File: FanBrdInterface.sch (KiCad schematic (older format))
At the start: 14 parts, among them J13 FanBrdConn, U14 SI8261ABC-IS, U15 SI8261ABC-IS, U16 SI8261ABC-IS, U17 SI8261ABC-IS

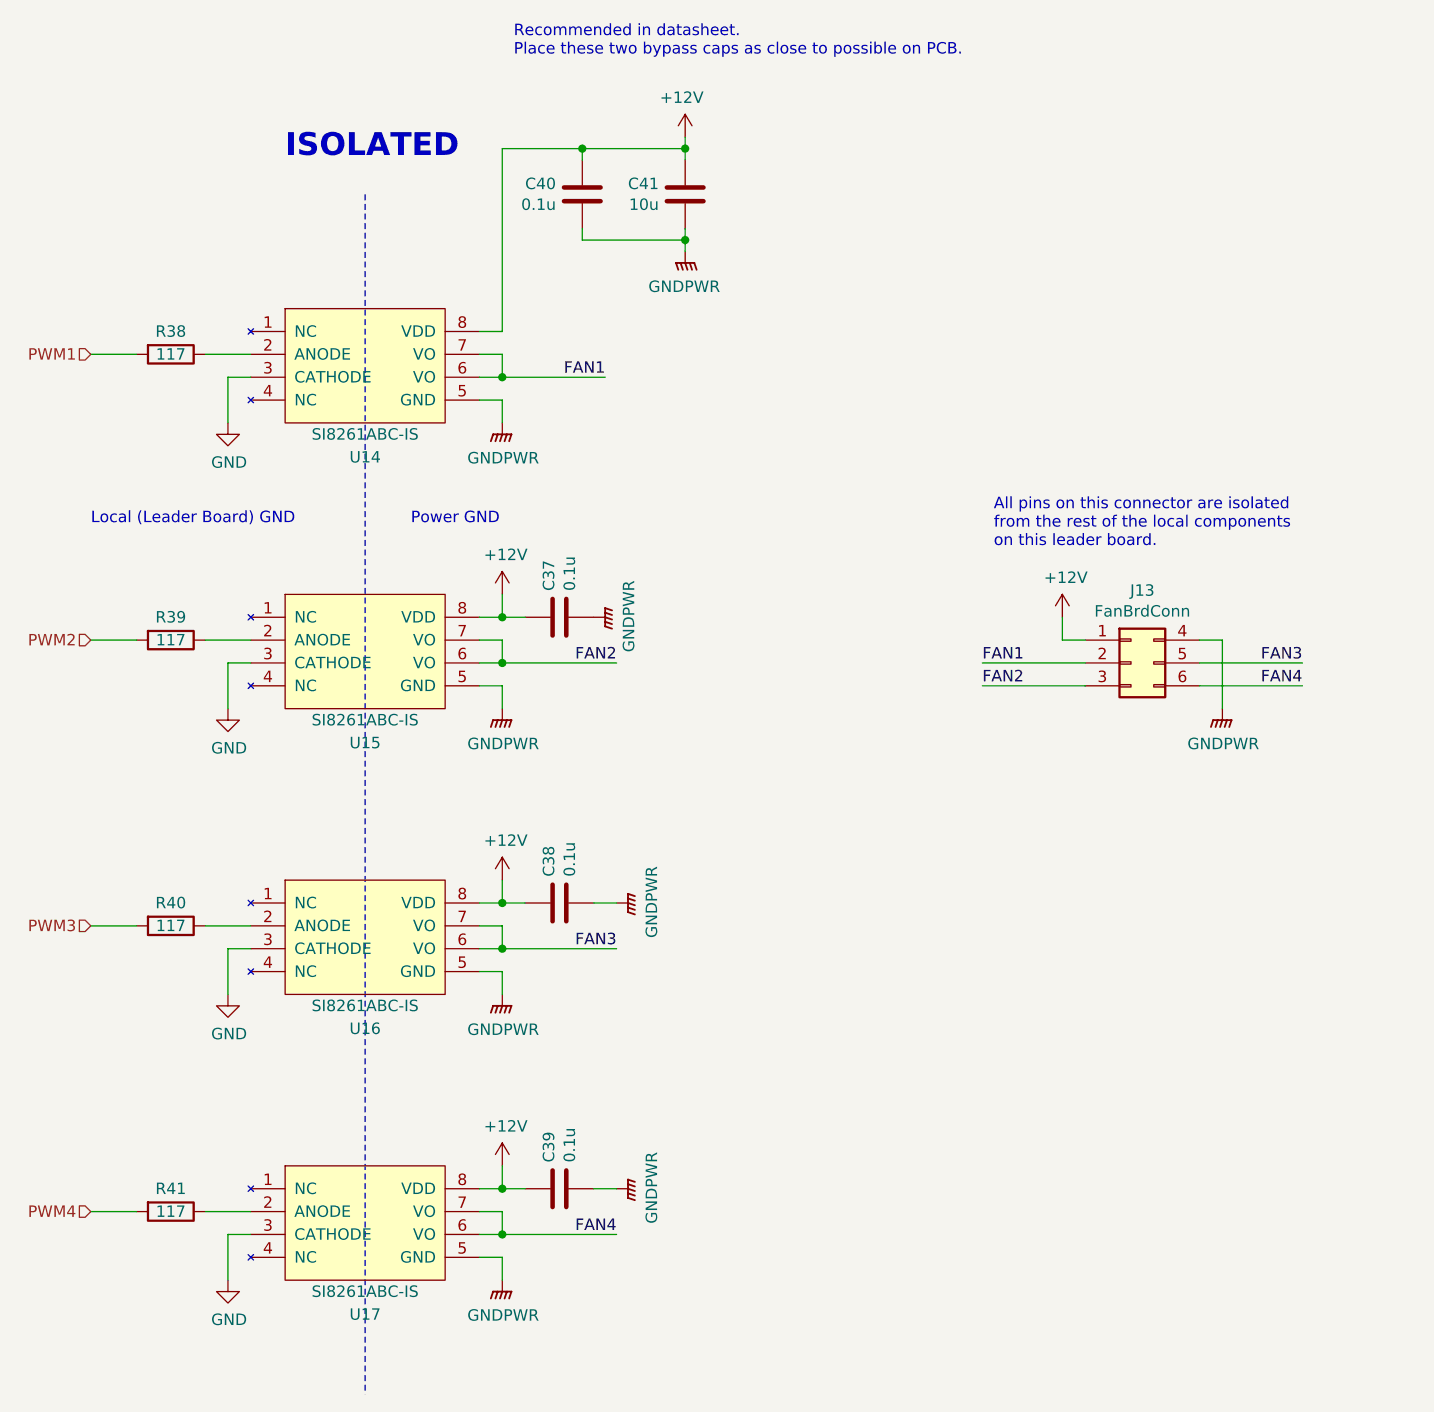
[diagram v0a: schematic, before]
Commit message: Moves BAS70-04 to utsvt-chips because other systems use this component
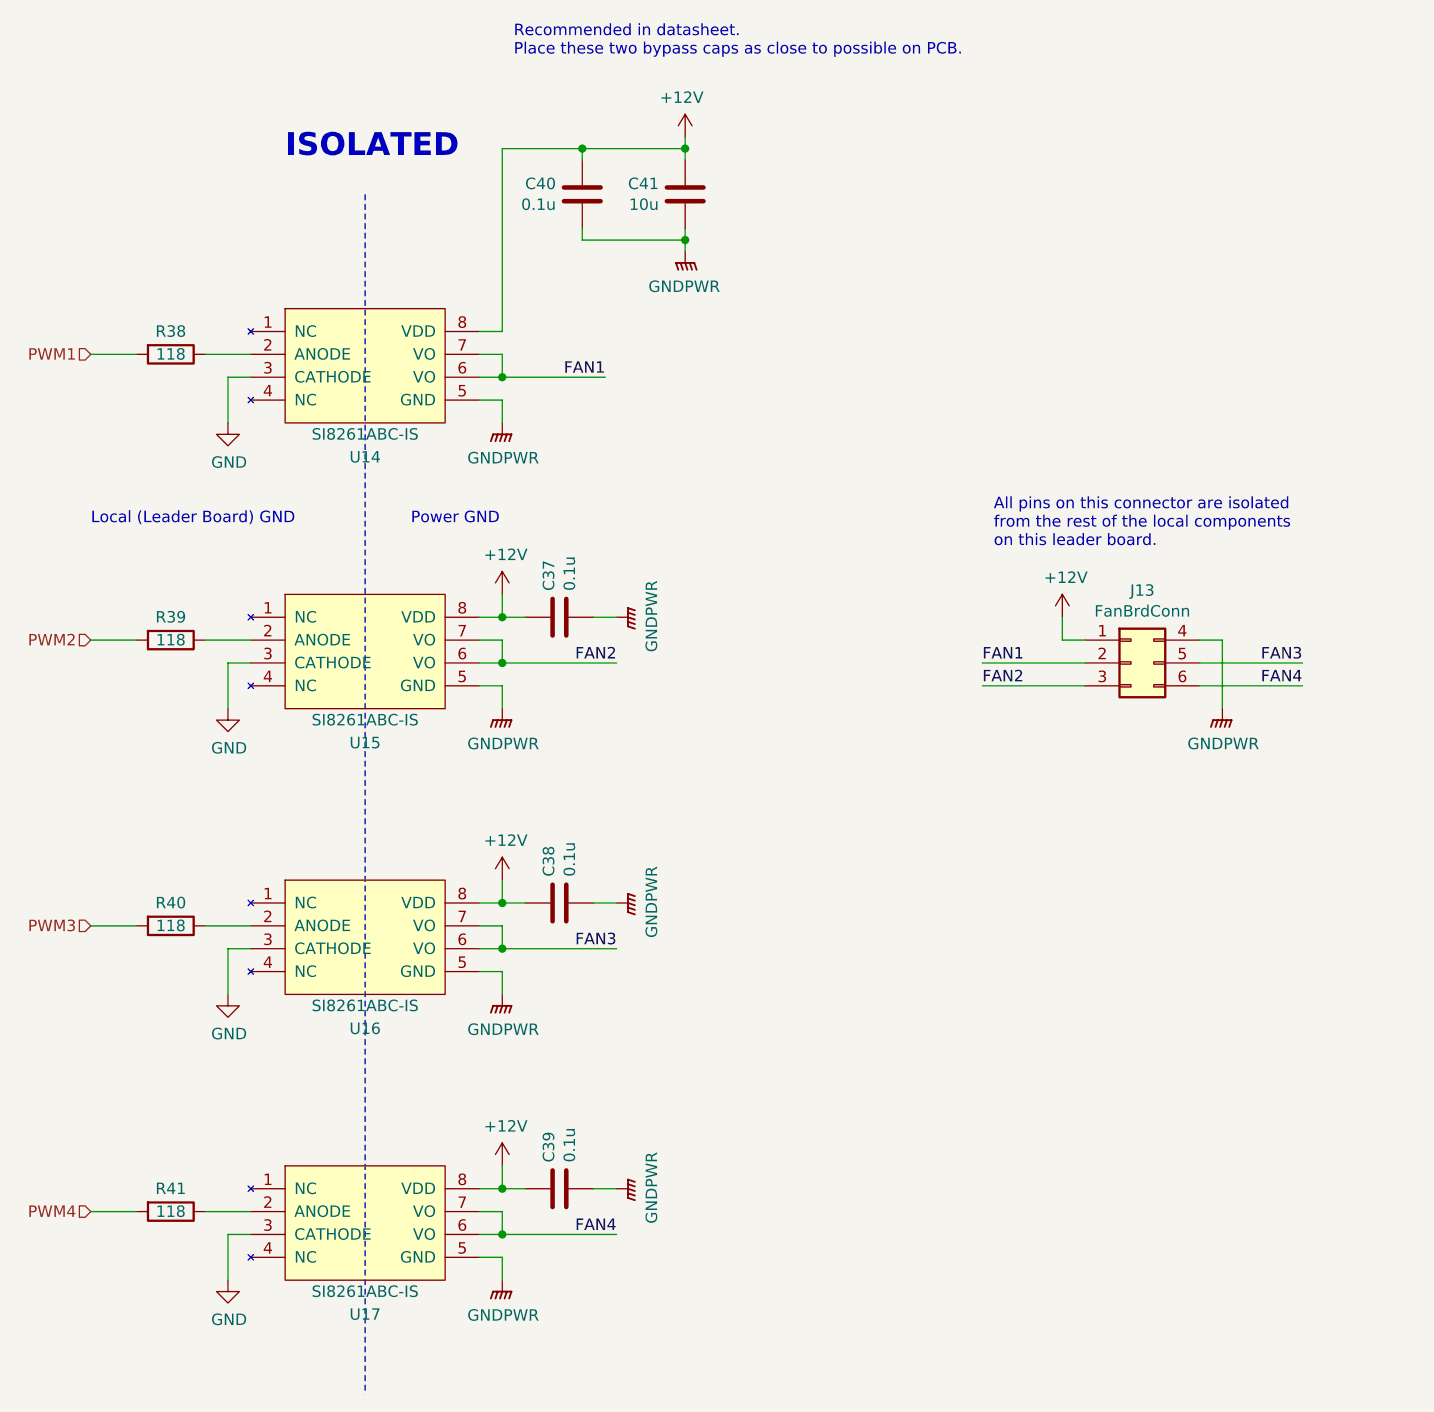
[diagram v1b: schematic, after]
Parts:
- R38, R39, R40, R41: value 117 -> 118
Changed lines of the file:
@@
 P 3400 2700
 F 0 "R38" V 3300 2700 50  0000 C CNN
-F 1 "117" V 3400 2700 50  0000 C CNN
+F 1 "118" V 3400 2700 50  0000 C CNN
 F 2 "Resistor_SMD:R_0805_2012Metric" V 3330 2700 50  0001 C CNN
 F 3 "~" H 3400 2700 50  0001 C CNN
@@
 P 3400 3950
 F 0 "R39" V 3300 3950 50  0000 C CNN
-F 1 "117" V 3400 3950 50  0000 C CNN
+F 1 "118" V 3400 3950 50  0000 C CNN
 F 2 "Resistor_SMD:R_0805_2012Metric" V 3330 3950 50  0001 C CNN
 F 3 "~" H 3400 3950 50  0001 C CNN
@@
 P 3400 5200
 F 0 "R40" V 3300 5200 50  0000 C CNN
-F 1 "117" V 3400 5200 50  0000 C CNN
+F 1 "118" V 3400 5200 50  0000 C CNN
 F 2 "Resistor_SMD:R_0805_2012Metric" V 3330 5200 50  0001 C CNN
 F 3 "~" H 3400 5200 50  0001 C CNN
@@
 P 3400 6450
 F 0 "R41" V 3300 6450 50  0000 C CNN
-F 1 "117" V 3400 6450 50  0000 C CNN
+F 1 "118" V 3400 6450 50  0000 C CNN
 F 2 "Resistor_SMD:R_0805_2012Metric" V 3330 6450 50  0001 C CNN
 F 3 "~" H 3400 6450 50  0001 C CNN
@@
 L power:GNDPWR #PWR?
 U 1 1 5F1DA30D
-P 5250 3850
+P 5350 3850
 AR Path="/5C38C674/5F1DA30D" Ref="#PWR?"  Part="1"
 AR Path="/5F145F02/5F1DA30D" Ref="#PWR091"  Part="1"
-F 0 "#PWR091" H 5250 3650 50  0001 C CNN
-F 1 "GNDPWR" H 5254 3696 50  0000 C CNN
-F 2 "" H 5250 3800 50  0001 C CNN
-F 3 "" H 5250 3800 50  0001 C CNN
-	1    5250 3850
+F 0 "#PWR091" H 5350 3650 50  0001 C CNN
+F 1 "GNDPWR" H 5354 3696 50  0000 C CNN
+F 2 "" H 5350 3800 50  0001 C CNN
+F 3 "" H 5350 3800 50  0001 C CNN
+	1    5350 3850
 	0    -1   -1   0
 $EndComp
@@
 Text Notes 4450 3450 0    50   ~ 0
 Power GND
+Wire Wire Line
+	5350 3850 5250 3850
 $EndSCHEMATC

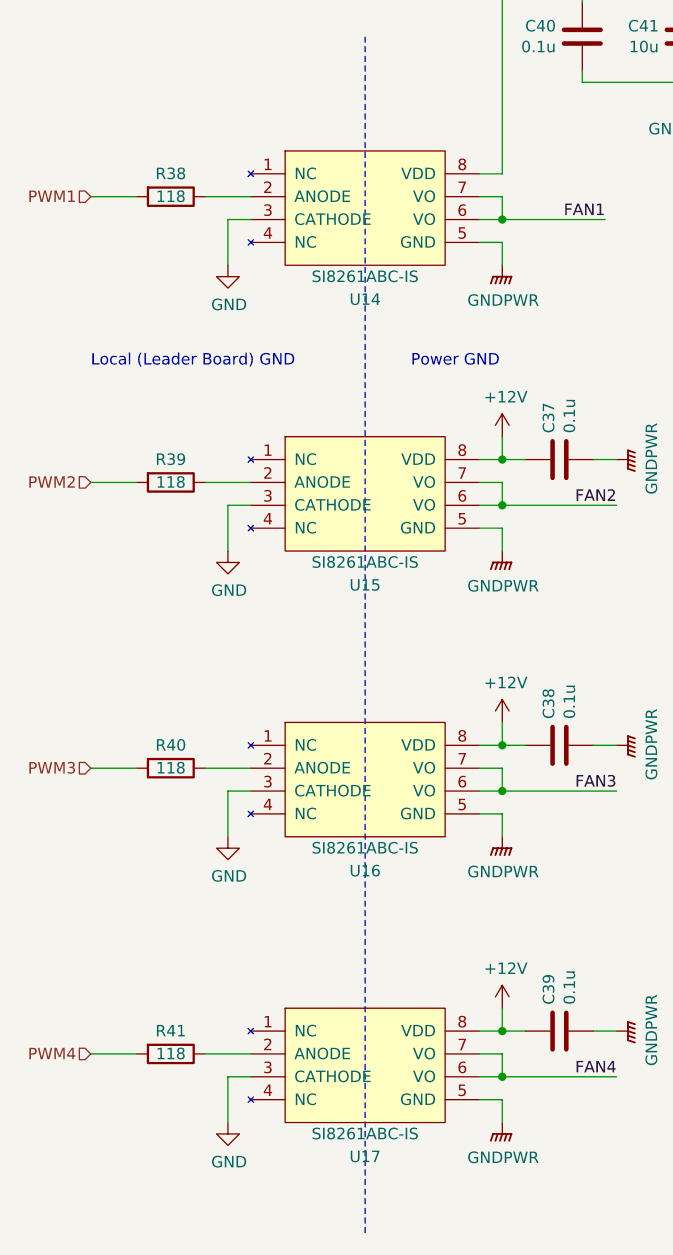
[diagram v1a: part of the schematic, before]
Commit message: Updates BAS70-04 footprint for Contactor auxillary interface
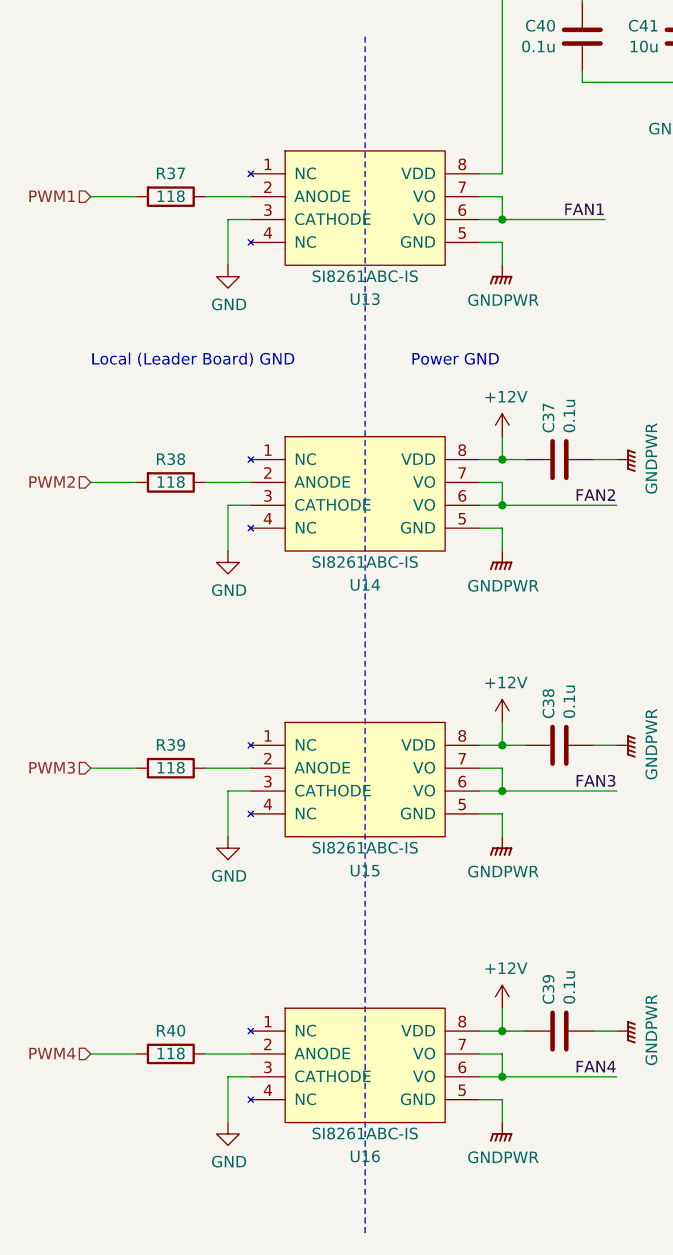
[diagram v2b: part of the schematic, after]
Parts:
- renumbered R38 to R37, R39 to R38, R40 to R39, R41 to R40, U14 to U13, U15 to U14, U16 to U15, U17 to U16
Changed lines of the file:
@@
 P 5650 1750
 AR Path="/5C38C674/5F130099" Ref="#PWR?"  Part="1"
-AR Path="/5F145F02/5F130099" Ref="#PWR094"  Part="1"
-F 0 "#PWR094" H 5650 1600 50  0001 C CNN
+AR Path="/5F145F02/5F130099" Ref="#PWR096"  Part="1"
+F 0 "#PWR096" H 5650 1600 50  0001 C CNN
 F 1 "+12V" H 5665 1923 50  0000 C CNN
 F 2 "" H 5650 1750 50  0001 C CNN
@@
 P 5650 2250
 AR Path="/5C38C674/5F1300F5" Ref="#PWR?"  Part="1"
-AR Path="/5F145F02/5F1300F5" Ref="#PWR095"  Part="1"
-F 0 "#PWR095" H 5650 2050 50  0001 C CNN
+AR Path="/5F145F02/5F1300F5" Ref="#PWR097"  Part="1"
+F 0 "#PWR097" H 5650 2050 50  0001 C CNN
 F 1 "GNDPWR" H 5654 2096 50  0000 C CNN
 F 2 "" H 5650 2200 50  0001 C CNN
@@
 P 4850 3000
 AR Path="/5C38C674/5F1300FB" Ref="#PWR?"  Part="1"
-AR Path="/5F145F02/5F1300FB" Ref="#PWR084"  Part="1"
-F 0 "#PWR084" H 4850 2800 50  0001 C CNN
+AR Path="/5F145F02/5F1300FB" Ref="#PWR086"  Part="1"
+F 0 "#PWR086" H 4850 2800 50  0001 C CNN
 F 1 "GNDPWR" H 4854 2846 50  0000 C CNN
 F 2 "" H 4850 2950 50  0001 C CNN
@@
 	4850 2700 4850 2800
 $Comp
-L power:GND #PWR080
+L power:GND #PWR082
 U 1 1 5F1328D9
 P 3650 3000
-F 0 "#PWR080" H 3650 2750 50  0001 C CNN
+F 0 "#PWR082" H 3650 2750 50  0001 C CNN
 F 1 "GND" H 3655 2827 50  0000 C CNN
 F 2 "" H 3650 3000 50  0001 C CNN
@@
 	3650 2800 3750 2800
 $Comp
-L utsvt-bps:SI8261ABC-IS U14
+L utsvt-bps:SI8261ABC-IS U13
 U 1 1 5F14B1DD
 P 4250 2500
-F 0 "U14" H 4250 1850 50  0000 C CNN
+F 0 "U13" H 4250 1850 50  0000 C CNN
 F 1 "SI8261ABC-IS" H 4250 1950 50  0000 C CNN
 F 2 "Package_SO:SOIC-8_3.9x4.9mm_P1.27mm" H 4250 2500 50  0001 C CNN
@@
 $EndComp
 $Comp
-L Device:R R38
+L Device:R R37
 U 1 1 5F14C350
 P 3400 2700
-F 0 "R38" V 3300 2700 50  0000 C CNN
+F 0 "R37" V 3300 2700 50  0000 C CNN
 F 1 "118" V 3400 2700 50  0000 C CNN
 F 2 "Resistor_SMD:R_0805_2012Metric" V 3330 2700 50  0001 C CNN
@@
 P 4850 3750
 AR Path="/5C38C674/5F1531CC" Ref="#PWR?"  Part="1"
-AR Path="/5F145F02/5F1531CC" Ref="#PWR085"  Part="1"
-F 0 "#PWR085" H 4850 3600 50  0001 C CNN
+AR Path="/5F145F02/5F1531CC" Ref="#PWR087"  Part="1"
+F 0 "#PWR087" H 4850 3600 50  0001 C CNN
 F 1 "+12V" H 4865 3923 50  0000 C CNN
 F 2 "" H 4850 3750 50  0001 C CNN
@@
 P 4850 4250
 AR Path="/5C38C674/5F1531F5" Ref="#PWR?"  Part="1"
-AR Path="/5F145F02/5F1531F5" Ref="#PWR086"  Part="1"
-F 0 "#PWR086" H 4850 4050 50  0001 C CNN
+AR Path="/5F145F02/5F1531F5" Ref="#PWR088"  Part="1"
+F 0 "#PWR088" H 4850 4050 50  0001 C CNN
 F 1 "GNDPWR" H 4854 4096 50  0000 C CNN
 F 2 "" H 4850 4200 50  0001 C CNN
@@
 	4850 3950 4850 4050
 $Comp
-L power:GND #PWR081
+L power:GND #PWR083
 U 1 1 5F1531FD
 P 3650 4250
-F 0 "#PWR081" H 3650 4000 50  0001 C CNN
+F 0 "#PWR083" H 3650 4000 50  0001 C CNN
 F 1 "GND" H 3655 4077 50  0000 C CNN
 F 2 "" H 3650 4250 50  0001 C CNN
@@
 	3650 4050 3750 4050
 $Comp
-L utsvt-bps:SI8261ABC-IS U15
+L utsvt-bps:SI8261ABC-IS U14
 U 1 1 5F153207
 P 4250 3750
-F 0 "U15" H 4250 3100 50  0000 C CNN
+F 0 "U14" H 4250 3100 50  0000 C CNN
 F 1 "SI8261ABC-IS" H 4250 3200 50  0000 C CNN
 F 2 "Package_SO:SOIC-8_3.9x4.9mm_P1.27mm" H 4250 3750 50  0001 C CNN
@@
 $EndComp
 $Comp
-L Device:R R39
+L Device:R R38
 U 1 1 5F15320D
 P 3400 3950
-F 0 "R39" V 3300 3950 50  0000 C CNN
+F 0 "R38" V 3300 3950 50  0000 C CNN
 F 1 "118" V 3400 3950 50  0000 C CNN
 F 2 "Resistor_SMD:R_0805_2012Metric" V 3330 3950 50  0001 C CNN
@@
 P 4850 5000
 AR Path="/5C38C674/5F155440" Ref="#PWR?"  Part="1"
-AR Path="/5F145F02/5F155440" Ref="#PWR087"  Part="1"
-F 0 "#PWR087" H 4850 4850 50  0001 C CNN
+AR Path="/5F145F02/5F155440" Ref="#PWR089"  Part="1"
+F 0 "#PWR089" H 4850 4850 50  0001 C CNN
 F 1 "+12V" H 4865 5173 50  0000 C CNN
 F 2 "" H 4850 5000 50  0001 C CNN
@@
 P 4850 5500
 AR Path="/5C38C674/5F155469" Ref="#PWR?"  Part="1"
-AR Path="/5F145F02/5F155469" Ref="#PWR088"  Part="1"
-F 0 "#PWR088" H 4850 5300 50  0001 C CNN
+AR Path="/5F145F02/5F155469" Ref="#PWR090"  Part="1"
+F 0 "#PWR090" H 4850 5300 50  0001 C CNN
 F 1 "GNDPWR" H 4854 5346 50  0000 C CNN
 F 2 "" H 4850 5450 50  0001 C CNN
@@
 	4850 5200 4850 5300
 $Comp
-L power:GND #PWR082
+L power:GND #PWR084
 U 1 1 5F155471
 P 3650 5500
-F 0 "#PWR082" H 3650 5250 50  0001 C CNN
+F 0 "#PWR084" H 3650 5250 50  0001 C CNN
 F 1 "GND" H 3655 5327 50  0000 C CNN
 F 2 "" H 3650 5500 50  0001 C CNN
@@
 	3650 5300 3750 5300
 $Comp
-L utsvt-bps:SI8261ABC-IS U16
+L utsvt-bps:SI8261ABC-IS U15
 U 1 1 5F15547B
 P 4250 5000
-F 0 "U16" H 4250 4350 50  0000 C CNN
+F 0 "U15" H 4250 4350 50  0000 C CNN
 F 1 "SI8261ABC-IS" H 4250 4450 50  0000 C CNN
 F 2 "Package_SO:SOIC-8_3.9x4.9mm_P1.27mm" H 4250 5000 50  0001 C CNN
@@
 $EndComp
 $Comp
-L Device:R R40
+L Device:R R39
 U 1 1 5F155481
 P 3400 5200
-F 0 "R40" V 3300 5200 50  0000 C CNN
+F 0 "R39" V 3300 5200 50  0000 C CNN
 F 1 "118" V 3400 5200 50  0000 C CNN
 F 2 "Resistor_SMD:R_0805_2012Metric" V 3330 5200 50  0001 C CNN
@@
 FAN3
 $Comp
-L power:+12V #PWR096
+L power:+12V #PWR098
 U 1 1 5F157D4C
 P 7300 3850
-F 0 "#PWR096" H 7300 3700 50  0001 C CNN
+F 0 "#PWR098" H 7300 3700 50  0001 C CNN
 F 1 "+12V" H 7315 4023 50  0000 C CNN
 F 2 "" H 7300 3850 50  0001 C CNN
@@
 P 8000 4250
 AR Path="/5C38C674/5F15A290" Ref="#PWR?"  Part="1"
-AR Path="/5F145F02/5F15A290" Ref="#PWR097"  Part="1"
-F 0 "#PWR097" H 8000 4050 50  0001 C CNN
+AR Path="/5F145F02/5F15A290" Ref="#PWR099"  Part="1"
+F 0 "#PWR099" H 8000 4050 50  0001 C CNN
 F 1 "GNDPWR" H 8004 4096 50  0000 C CNN
 F 2 "" H 8000 4200 50  0001 C CNN
@@
 P 4850 6250
 AR Path="/5C38C674/5F1644DE" Ref="#PWR?"  Part="1"
-AR Path="/5F145F02/5F1644DE" Ref="#PWR089"  Part="1"
-F 0 "#PWR089" H 4850 6100 50  0001 C CNN
+AR Path="/5F145F02/5F1644DE" Ref="#PWR091"  Part="1"
+F 0 "#PWR091" H 4850 6100 50  0001 C CNN
 F 1 "+12V" H 4865 6423 50  0000 C CNN
 F 2 "" H 4850 6250 50  0001 C CNN
@@
 P 4850 6750
 AR Path="/5C38C674/5F164507" Ref="#PWR?"  Part="1"
-AR Path="/5F145F02/5F164507" Ref="#PWR090"  Part="1"
-F 0 "#PWR090" H 4850 6550 50  0001 C CNN
+AR Path="/5F145F02/5F164507" Ref="#PWR092"  Part="1"
+F 0 "#PWR092" H 4850 6550 50  0001 C CNN
 F 1 "GNDPWR" H 4854 6596 50  0000 C CNN
 F 2 "" H 4850 6700 50  0001 C CNN
@@
 	4850 6450 4850 6550
 $Comp
-L power:GND #PWR083
+L power:GND #PWR085
 U 1 1 5F16450F
 P 3650 6750
-F 0 "#PWR083" H 3650 6500 50  0001 C CNN
+F 0 "#PWR085" H 3650 6500 50  0001 C CNN
 F 1 "GND" H 3655 6577 50  0000 C CNN
 F 2 "" H 3650 6750 50  0001 C CNN
@@
 	3650 6550 3750 6550
 $Comp
-L utsvt-bps:SI8261ABC-IS U17
+L utsvt-bps:SI8261ABC-IS U16
 U 1 1 5F164519
 P 4250 6250
-F 0 "U17" H 4250 5600 50  0000 C CNN
+F 0 "U16" H 4250 5600 50  0000 C CNN
 F 1 "SI8261ABC-IS" H 4250 5700 50  0000 C CNN
 F 2 "Package_SO:SOIC-8_3.9x4.9mm_P1.27mm" H 4250 6250 50  0001 C CNN
@@
 $EndComp
 $Comp
-L Device:R R41
+L Device:R R40
 U 1 1 5F16451F
 P 3400 6450
-F 0 "R41" V 3300 6450 50  0000 C CNN
+F 0 "R40" V 3300 6450 50  0000 C CNN
 F 1 "118" V 3400 6450 50  0000 C CNN
 F 2 "Resistor_SMD:R_0805_2012Metric" V 3330 6450 50  0001 C CNN
@@
 P 5350 6350
 AR Path="/5C38C674/5F1D20B3" Ref="#PWR?"  Part="1"
-AR Path="/5F145F02/5F1D20B3" Ref="#PWR093"  Part="1"
-F 0 "#PWR093" H 5350 6150 50  0001 C CNN
+AR Path="/5F145F02/5F1D20B3" Ref="#PWR095"  Part="1"
+F 0 "#PWR095" H 5350 6150 50  0001 C CNN
 F 1 "GNDPWR" H 5354 6196 50  0000 C CNN
 F 2 "" H 5350 6300 50  0001 C CNN
@@
 P 5350 5100
 AR Path="/5C38C674/5F1D596F" Ref="#PWR?"  Part="1"
-AR Path="/5F145F02/5F1D596F" Ref="#PWR092"  Part="1"
-F 0 "#PWR092" H 5350 4900 50  0001 C CNN
+AR Path="/5F145F02/5F1D596F" Ref="#PWR094"  Part="1"
+F 0 "#PWR094" H 5350 4900 50  0001 C CNN
 F 1 "GNDPWR" H 5354 4946 50  0000 C CNN
 F 2 "" H 5350 5050 50  0001 C CNN
@@
 P 5350 3850
 AR Path="/5C38C674/5F1DA30D" Ref="#PWR?"  Part="1"
-AR Path="/5F145F02/5F1DA30D" Ref="#PWR091"  Part="1"
-F 0 "#PWR091" H 5350 3650 50  0001 C CNN
+AR Path="/5F145F02/5F1DA30D" Ref="#PWR093"  Part="1"
+F 0 "#PWR093" H 5350 3650 50  0001 C CNN
 F 1 "GNDPWR" H 5354 3696 50  0000 C CNN
 F 2 "" H 5350 3800 50  0001 C CNN
